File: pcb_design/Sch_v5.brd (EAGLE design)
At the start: 85.1 x 49.5 mm, 32 parts

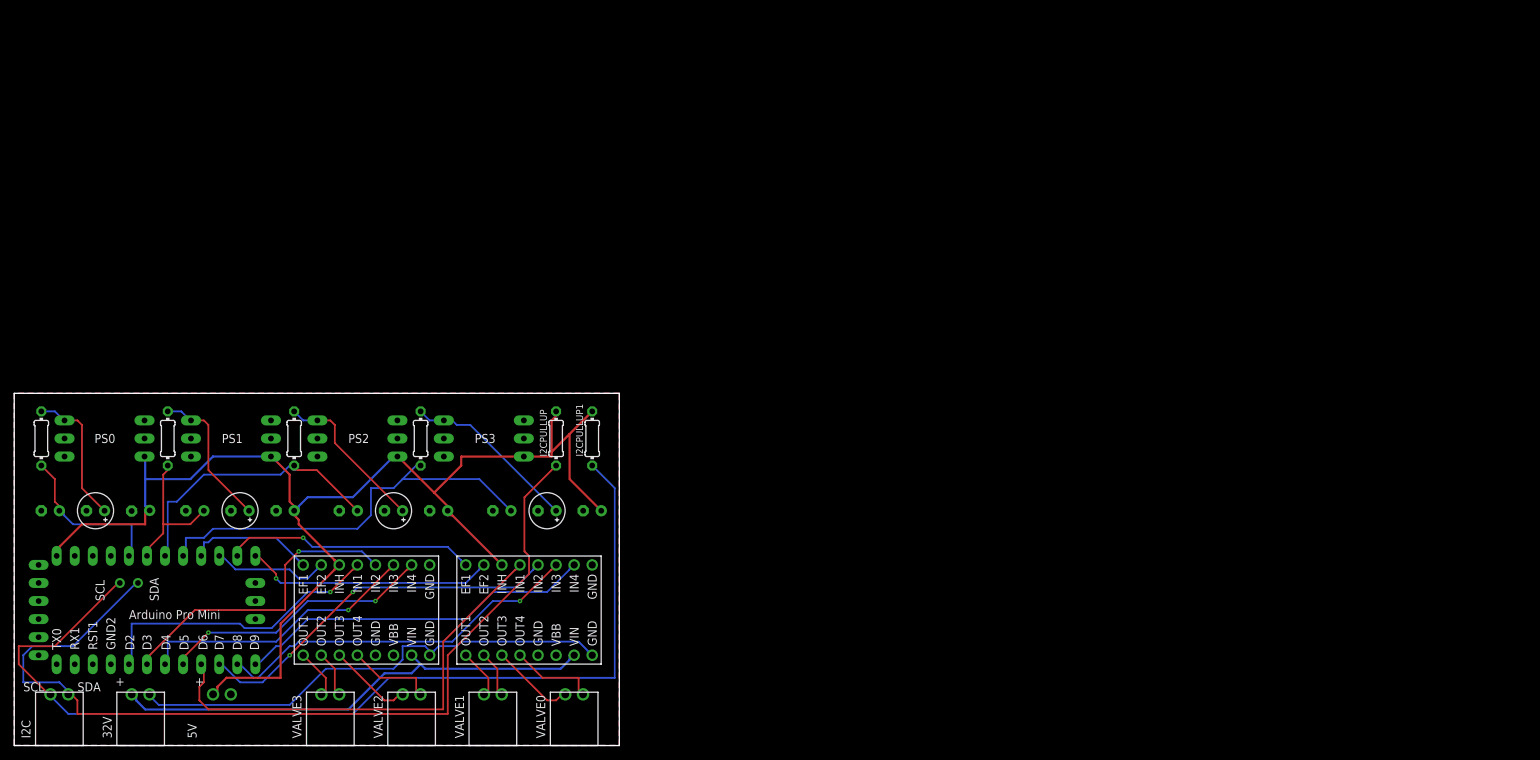
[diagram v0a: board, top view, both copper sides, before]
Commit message: adding M3 mounting holes with no solder mask
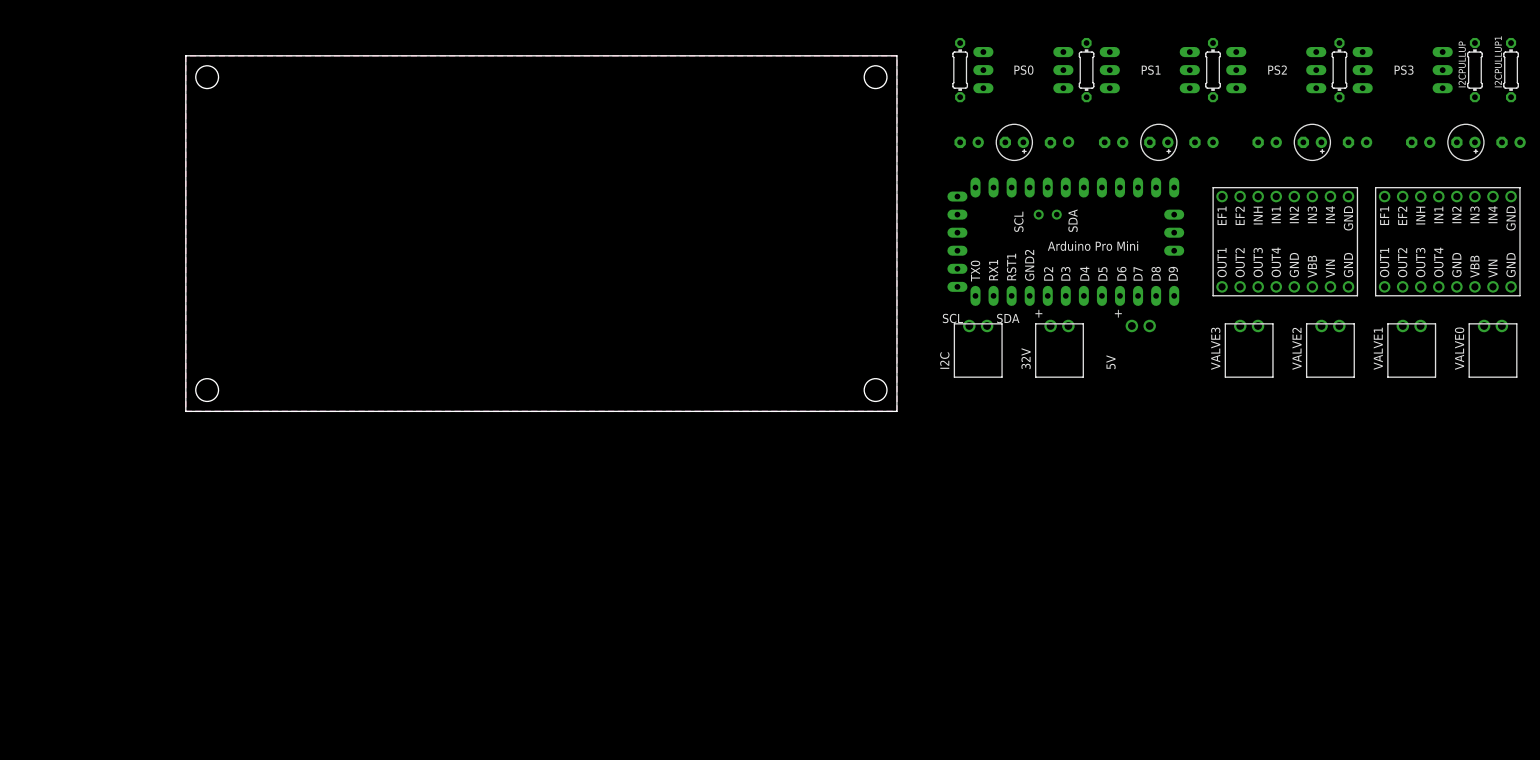
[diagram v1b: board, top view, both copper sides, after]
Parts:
- moved 32V 139.2 mm to (122.9, 4.81)
- moved C1 139.2 mm to (116.5, 37.8)
- moved C2 139.2 mm to (136.8, 37.8)
- moved C5 139.2 mm to (122.9, 37.8)
- moved C6 139.2 mm to (143.2, 37.8)
- moved C7 139.2 mm to (164.8, 37.8)
- moved C8 139.2 mm to (186.4, 37.8)
- moved C9 139.2 mm to (110.2, 37.8)
- moved I2C 139.2 mm to (111.4, 4.81)
- moved I2CPULLUP 139.2 mm to (181.3, 48.0)
- moved I2CPULLUP1 139.2 mm to (186.4, 48.0)
- moved PS0 139.2 mm to (117.8, 48.0)
- moved PS1 139.2 mm to (135.6, 48.0)
- moved PS2 139.2 mm to (153.3, 48.0)
- moved PS3 139.2 mm to (171.1, 48.0)
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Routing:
- net VDD: track 181.1 -> 0.00 mm
- net N$21: track 140.9 -> 0.00 mm
- net N$9: track 129.4 -> 0.00 mm
- net GND2: track 70.4 -> 0.00 mm
- net VIN: track 69.3 -> 0.00 mm
- net D6: track 65.7 -> 0.00 mm
- net A3: track 59.5 -> 0.00 mm
- net D7: track 53.1 -> 0.00 mm, vias 2 -> 0
- net D8: track 52.6 -> 0.00 mm, vias 1 -> 0
- net D9: track 51.0 -> 0.00 mm
- net D3: track 44.3 -> 0.00 mm, vias 1 -> 0
- net D2: track 42.2 -> 0.00 mm, vias 1 -> 0
- net D4: track 40.1 -> 0.00 mm, vias 1 -> 0
- net A2: track 39.8 -> 0.00 mm
- net D5: track 39.0 -> 0.00 mm, vias 2 -> 0
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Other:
- board size 85.1 x 49.5 mm -> 100 x 50 mm

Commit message: added byu parts library
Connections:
- net GND2 renamed MOTOR_GND
- net N$21 renamed SCL
- net N$9 renamed SDA
- net VIN renamed MOTOR_VDD
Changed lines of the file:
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@@
 <drawing>
 <settings>
-<setting alwaysvectorfont="no"/>
+<setting alwaysvectorfont="yes"/>
 <setting verticaltext="up"/>
 </settings>
@@
 </class>
 <class number="1" name="Power" width="0.3048" drill="0">
+<clearance class="1" value="0.508"/>
 </class>
-<class number="2" name="GND" width="0" drill="0">
+<class number="2" name="Motor Power" width="0.3048" drill="0">
+<clearance class="2" value="1.27"/>
 </class>
-<class number="3" name="Motor Power" width="0.3048" drill="0">
-<clearance class="3" value="0.0508"/>
+<class number="3" name="Analog Signal" width="0" drill="0">
+<clearance class="3" value="0.254"/>
+</class>
+<class number="4" name="I2C Bus" width="0" drill="0">
 </class>
 </classes>
@@
 </elements>
 <signals>
-<signal name="GND" class="3">
+<signal name="GND">
 <contactref element="PS1" pad="1"/>
 <contactref element="C6" pad="-"/>
@@
 <wire x1="153.34" y1="17.51" x2="162.21" y2="12.01" width="0" layer="19" extent="1-1"/>
 </signal>
-<signal name="VIN" class="3">
+<signal name="MOTOR_VDD" class="2">
 <contactref element="U$3" pad="7"/>
 <contactref element="U$2" pad="7"/>
@@
 <wire x1="121.61" y1="12.01" x2="160.96" y2="17.51" width="0" layer="19" extent="1-1"/>
 </signal>
-<signal name="GND2">
+<signal name="MOTOR_GND">
 <contactref element="U$3" pad="8"/>
 <contactref element="U$2" pad="8"/>
@@
 <wire x1="124.11" y1="12.01" x2="163.5" y2="17.51" width="0" layer="19" extent="1-1"/>
 </signal>
-<signal name="N$21">
+<signal name="SCL" class="4">
 <contactref element="U$1" pad="A5"/>
 <contactref element="I2C" pad="1"/>
@@
 <wire x1="150.78" y1="12.01" x2="148.26" y2="17.51" width="0" layer="19" extent="1-1"/>
 </signal>
-<signal name="A0">
+<signal name="A0" class="3">
 <contactref element="U$1" pad="A0"/>
 <contactref element="R1" pad="2"/>
 <contactref element="C9" pad="+"/>
-<wire x1="111.43" y1="37.83" x2="108.89" y2="44.18" width="0" layer="19" extent="1-1"/>
-<wire x1="121.209" y1="31.48" x2="111.43" y2="37.83" width="0" layer="19" extent="1-1"/>
-</signal>
-<signal name="A1">
+<wire x1="111.43" y1="37.83" x2="121.209" y2="31.48" width="0" layer="19" extent="1-1"/>
+<wire x1="108.89" y1="44.18" x2="111.43" y2="37.83" width="0" layer="19" extent="1-1"/>
+</signal>
+<signal name="A1" class="3">
 <contactref element="U$1" pad="A1"/>
 <contactref element="R2" pad="2"/>
@@
 <wire x1="123.749" y1="31.48" x2="131.75" y2="37.83" width="0" layer="19" extent="1-1"/>
 </signal>
-<signal name="A2">
+<signal name="A2" class="3">
 <contactref element="U$1" pad="A2"/>
 <contactref element="R3" pad="2"/>
 <contactref element="C11" pad="+"/>
-<wire x1="153.34" y1="37.83" x2="144.45" y2="44.18" width="0" layer="19" extent="1-1"/>
+<wire x1="144.45" y1="44.18" x2="153.34" y2="37.83" width="0" layer="19" extent="1-1"/>
 <wire x1="126.289" y1="31.48" x2="144.45" y2="44.18" width="0" layer="19" extent="1-1"/>
 </signal>
-<signal name="A3">
+<signal name="A3" class="3">
 <contactref element="U$1" pad="A3"/>
 <contactref element="R4" pad="2"/>
@@
 <wire x1="131.369" y1="16.24" x2="176.2" y2="30.21" width="0" layer="19" extent="1-1"/>
 </signal>
-<signal name="N$9">
+<signal name="SDA" class="4">
 <contactref element="I2C" pad="2"/>
 <contactref element="U$1" pad="A4"/>

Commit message: commiting recent work
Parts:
- removed 32V, 5V, I2C: 1778625, 1778625:1778625
- removed I2CPULLUP, I2CPULLUP1: (no value), rcl:0204/7
- removed U$1: ABK-PRO-MINI, Arduino-clone:ABK-PRO-MINI
- removed U$2, U$3: A4990, pololu-stepper-driver:A4990
- added 12V_IN, I2C_IN, I2C_OUT: PHOENIX_CONNECTOR_1778625, byu_pressure_control:PHOENIX_CONNECTOR_1778625
- added DRIVER_A, DRIVER_B: A4990_DUAL_MOTOR_DRIVER_CARRIER, byu_pressure_control:A4990_DUAL_MOTOR_DRIVER_CARRIER
- added NANO: ARDUINO_NANO_EVERY, byu_pressure_control:NANO_FOOTPRINT
- C1, C10, C11, C12, C2, C3, C4, C5, C6, C7, C8, C9: device rcl:E2,5-5 -> byu_pressure_control:CERAMIC_CAPACITOR
- PS0, PS1, PS2, PS3: value (none) -> PRESSURE_SENSOR_ABPDRNN100PGAA5; device RAD_2:ABPDRNN100PGAA5 -> byu_pressure_control:PRESSURE_SENSOR_ABPDRNN100PGAA5
- R1, R2, R3, R4: value 12kohm -> 12k
- VALVE0, VALVE1, VALVE2, VALVE3: value 1778625 -> PHOENIX_CONNECTOR_1778625; device 1778625:1778625 -> byu_pressure_control:PHOENIX_CONNECTOR_1778625
- moved C12 168.2 mm to (5.50, 37.5), flipped to the top, turned to 90 degrees
- moved C4 167.6 mm to (12.4, 37.5), turned to 90 degrees
- moved PS3 159.1 mm to (12.0, 50.0), flipped to the top, turned to 270 degrees
- moved R4 154.0 mm to (8.23, 46.2)
- moved VALVE3 134.6 mm to (15.0, -0.19)
- moved VALVE2 126.5 mm to (34.6, -0.19)
- moved C11 125.9 mm to (26.1, 37.5), flipped to the top, turned to 90 degrees
- moved C8 125.8 mm to (60.6, 37.5), flipped to the top, turned to 90 degrees
- moved C3 125.4 mm to (33.0, 37.5), turned to 90 degrees
- moved PS2 121.7 mm to (31.7, 50.0), flipped to the top, turned to 270 degrees
- moved VALVE1 118.3 mm to (54.2, -0.19)
- moved R3 116.3 mm to (28.1, 46.2)
- moved VALVE0 110.1 mm to (73.8, -0.19)
- moved C5 103.6 mm to (19.3, 37.5), flipped to the top, turned to 90 degrees
- moved C6 103.3 mm to (39.9, 37.5), flipped to the top, turned to 90 degrees
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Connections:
- removed net E1: U$1.D13, U$3.16
- removed net E2: U$1.D12, U$3.15
- removed net E3: U$1.D11, U$2.16
- removed net E4: U$1.D10, U$2.15
- removed net MOTOR_VDD: 32V.1, U$2.7, U$3.7
- removed net N$13: U$3.1, VALVE3.1
- removed net N$14: U$3.2, VALVE3.2
- removed net N$15: U$3.3, VALVE2.1
- removed net N$16: U$3.4, VALVE2.2
- removed net VDD: 5V.2, C5.+, C6.+, C7.+, C8.+, I2CPULLUP.2, I2CPULLUP1.2, PS0.6, PS1.6, PS2.6, PS3.6, U$1.RAW, U$2.14, U$3.14
- new net 12V: 12V_IN.1, DRIVER_A.10, DRIVER_B.10, NANO.15
- new net 5V: C5.2, C6.2, C7.2, C8.2, DRIVER_A.3, DRIVER_B.3, NANO.12, PS0.6, PS1.6, PS2.6, PS3.6
- new net EF1_A: DRIVER_A.1, NANO.28
- new net EF1_B: DRIVER_B.1, NANO.30
- new net EF2_A: DRIVER_A.2, NANO.29
- new net EF2_B: DRIVER_B.2, NANO.11
- new net N$10: DRIVER_B.15, VALVE3.2
- new net N$11: DRIVER_B.14, VALVE2.1
- new net N$12: DRIVER_B.13, VALVE2.2
- new net N$9: DRIVER_B.16, VALVE3.1
- net A0: now also C9.1, NANO.4; no longer C9.+, U$1.A0
- net A1: now also C10.1, NANO.5; no longer C10.+, U$1.A1
- net A2: now also C11.1, NANO.6; no longer C11.+, U$1.A2
- net A3: now also C12.1, NANO.7; no longer C12.+, U$1.A3
- net D2: now also DRIVER_B.4, NANO.20; no longer U$1.D2, U$3.13
- net D3: now also DRIVER_B.5, NANO.21; no longer U$1.D3, U$3.12
- net D4: now also DRIVER_B.6, NANO.22; no longer U$1.D4, U$3.11
- net D5: now also DRIVER_B.7, NANO.23; no longer U$1.D5, U$3.10
- net D6: now also DRIVER_A.4, NANO.24; no longer U$1.D6, U$2.13
- net D7: now also DRIVER_A.5, NANO.25; no longer U$1.D7, U$2.12
- net D8: now also DRIVER_A.6, NANO.26; no longer U$1.D8, U$2.11
- net D9: now also DRIVER_A.7, NANO.27; no longer U$1.D9, U$2.10
- net GND: now also C1.2, C10.2, C11.2, C12.2, C2.2, C3.2, C4.2, C5.1, C6.1, C7.1, C8.1, C9.2, DRIVER_A.12, DRIVER_A.8, DRIVER_B.12, DRIVER_B.8, NANO.14, NANO.19; no longer 5V.1, C1.-, C10.-, C11.-, C12.-, C2.-, C3.-, C4.-, C5.-, C6.-, C7.-, C8.-, C9.-, U$1.GND, U$2.9, U$3.9
- net MOTOR_GND: now also 12V_IN.2, DRIVER_A.9, DRIVER_B.9; no longer 32V.2, U$2.8, U$3.8
- net N$1: now also C1.1; no longer C1.+
- net N$2: now also C2.1; no longer C2.+
- net N$3: now also C3.1; no longer C3.+
- net N$4: now also C4.1; no longer C4.+
- net N$5: now also DRIVER_A.15; no longer U$2.2
- net N$6: now also DRIVER_A.16; no longer U$2.1
- net N$7: now also DRIVER_A.14; no longer U$2.3
- net N$8: now also DRIVER_A.13; no longer U$2.4
- net SCL: now also I2C_IN.1, I2C_OUT.1, NANO.9; no longer I2C.1, I2CPULLUP1.1, U$1.A5
- net SDA: now also I2C_IN.2, I2C_OUT.2, NANO.8; no longer I2C.2, I2CPULLUP.1, U$1.A4
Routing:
- added copper zone on layer 16, net MOTOR_GND
- removed copper zone on layer 16, net GND
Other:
- board size 100 x 50 mm -> 93 x 53 mm
- board text added: "BYU RaD Lab"
- board text added: "v5"
- board text removed: "Arduino Pro Mini"
- board text removed: "D2"
- board text removed: "D3"
- board text removed: "D4"
- board text removed: "D5"
- board text removed: "D6"
- board text removed: "D7"
- board text removed: "D8"
- board text removed: "D9"
- board text removed: "GND2"
- board text removed: "RST1"
- board text removed: "RX1"
- board text removed: "SDA"
- board text removed: "TX0"

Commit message: board routed
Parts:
- moved DRIVER_B 2.83 mm to (24.0, 28.0)
- moved I2C_OUT 2.69 mm to (92.0, 33.5)
- moved 12V_IN 2.06 mm to (-2.00, 14.8)
- moved DRIVER_A 2.06 mm to (43.5, 28.0)
- moved I2C_IN 2.00 mm to (-2.07, 24.9)
- moved VALVE0 1.50 mm to (73.8, -1.69)
- moved VALVE1 1.50 mm to (54.2, -1.69)
- moved VALVE2 1.50 mm to (34.6, -1.69)
- moved VALVE3 1.50 mm to (15.0, -1.69)
- moved C1 1.00 mm to (67.4, 38.5)
- moved C10 1.00 mm to (46.8, 38.5)
- moved C11 1.00 mm to (26.1, 38.5)
- moved C12 1.00 mm to (5.50, 38.5)
- moved C2 1.00 mm to (53.7, 38.5)
- moved C3 1.00 mm to (33.0, 38.5)
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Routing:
- net 5V: track 0.00 -> 136.3 mm, vias 0 -> 1
- net SDA: track 0.00 -> 100.9 mm
- net SCL: track 0.00 -> 92.1 mm
- net A3: track 0.00 -> 76.6 mm
- net EF1_B: track 0.00 -> 70.4 mm
- net A2: track 0.00 -> 66.3 mm
- net 12V: track 0.00 -> 63.0 mm
- net D5: track 0.00 -> 54.7 mm
- net N$8: track 0.00 -> 52.7 mm
- net EF2_B: track 0.00 -> 51.7 mm
- net D3: track 0.00 -> 50.9 mm
- net EF2_A: track 0.00 -> 49.0 mm
- net N$7: track 0.00 -> 47.8 mm, vias 0 -> 1
- net D4: track 0.00 -> 47.5 mm, vias 0 -> 1
- net D2: track 0.00 -> 45.1 mm
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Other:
- board size 93 x 53 mm -> 90 x 54 mm

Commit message: final version of pcb I think
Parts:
- removed NANO: ARDUINO_NANO_EVERY, byu_pressure_control:NANO_FOOTPRINT
- added NANO1: ARDUINO_NANO_EVERY, byu_pressure_control:ARDUINO_NANO_EVERY
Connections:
- net 12V: now also DRIVER_A.7, DRIVER_B.7, NANO1.15; no longer DRIVER_A.10, DRIVER_B.10, NANO.15
- net 5V: now also DRIVER_A.14, DRIVER_B.14, NANO1.12; no longer DRIVER_A.3, DRIVER_B.3, NANO.12
- net A0: now also NANO1.4; no longer NANO.4
- net A1: now also NANO1.5; no longer NANO.5
- net A2: now also NANO1.6; no longer NANO.6
- net A3: now also NANO1.7; no longer NANO.7
- net D2: now also DRIVER_B.13, NANO1.20; no longer DRIVER_B.4, NANO.20
- net D3: now also DRIVER_B.12, NANO1.21; no longer DRIVER_B.5, NANO.21
- net D4: now also DRIVER_B.11, NANO1.22; no longer DRIVER_B.6, NANO.22
- net D5: now also DRIVER_B.10, NANO1.23; no longer DRIVER_B.7, NANO.23
- net D6: now also DRIVER_A.13, NANO1.24; no longer DRIVER_A.4, NANO.24
- net D7: now also DRIVER_A.12, NANO1.25; no longer DRIVER_A.5, NANO.25
- net D8: now also DRIVER_A.11, NANO1.26; no longer DRIVER_A.6, NANO.26
- net D9: now also DRIVER_A.10, NANO1.27; no longer DRIVER_A.7, NANO.27
- net EF1_A: now also DRIVER_A.16, NANO1.28; no longer DRIVER_A.1, NANO.28
- net EF1_B: now also DRIVER_B.16, NANO1.30; no longer DRIVER_B.1, NANO.30
- net EF2_A: now also DRIVER_A.15, NANO1.29; no longer DRIVER_A.2, NANO.29
- net EF2_B: now also DRIVER_B.15, NANO1.11; no longer DRIVER_B.2, NANO.11
- net GND: now also DRIVER_A.5, DRIVER_A.9, DRIVER_B.5, DRIVER_B.9, NANO1.14, NANO1.19; no longer DRIVER_A.12, DRIVER_A.8, DRIVER_B.12, DRIVER_B.8, NANO.14, NANO.19
- net MOTOR_GND: now also DRIVER_A.8, DRIVER_B.8; no longer DRIVER_A.9, DRIVER_B.9
- net N$10: now also DRIVER_B.2; no longer DRIVER_B.15
- net N$11: now also DRIVER_B.3; no longer DRIVER_B.14
- net N$12: now also DRIVER_B.4; no longer DRIVER_B.13
- net N$5: now also DRIVER_A.2; no longer DRIVER_A.15
- net N$6: now also DRIVER_A.1; no longer DRIVER_A.16
- net N$7: now also DRIVER_A.3; no longer DRIVER_A.14
- net N$8: now also DRIVER_A.4; no longer DRIVER_A.13
- net N$9: now also DRIVER_B.1; no longer DRIVER_B.16
- net SCL: now also NANO1.9; no longer NANO.9
- net SDA: now also NANO1.8; no longer NANO.8
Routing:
- net D4: track 47.5 -> 74.5 mm
- net EF1_A: track 38.7 -> 58.3 mm
- net D5: track 54.7 -> 72.3 mm
- net 12V: track 63.0 -> 79.8 mm
- net EF2_B: track 51.7 -> 67.9 mm, vias 0 -> 1
- net N$7: track 47.8 -> 34.0 mm, vias 1 -> 0
- net N$8: track 52.7 -> 39.4 mm
- net N$11: track 26.9 -> 14.2 mm
- net N$6: track 24.9 -> 12.3 mm
- net D6: track 30.5 -> 43.0 mm
- net D7: track 33.7 -> 46.2 mm
- net D8: track 37.3 -> 49.7 mm
- net D9: track 40.9 -> 53.3 mm, vias 0 -> 1
- net N$5: track 28.4 -> 16.6 mm
- net 5V: track 136.3 -> 148.1 mm, vias 1 -> 0
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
